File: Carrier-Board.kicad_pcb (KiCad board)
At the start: 4 copper layers, 92 x 96 mm, 50 parts, among them J1 CONN_3-6318491-6, J10 Conn_02x03_Odd_Even, J2 Conn_01x0, J3 Conn_02x26_Odd_Even, J4 SI-51009-F, J5 Conn_02x26_Odd_Even, J6 Conn_01x03_Male, J7 Conn_01x03_Male, J8 Conn_01x06_Male, J9 Conn_02x04_Odd_Even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

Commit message: asdf
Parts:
- removed C1, C3: 10uF, Capacitors_SMD:C_0805
- removed C2, C4: 22uF, Capacitors_SMD:C_0805
- removed C27, C28, C29: .1uF, Capacitors_SMD:C_0603
- removed D5: D_Zener 9V, Diodes_SMD:D_SOD-323
- removed D6, D7, D8: LED, Diodes_SMD:D_1206
- removed G1 (x2): LOGO, BusSimulator:LetSatLogo440
- removed J10: Conn_02x03_Odd_Even, Pin_Headers:Pin_Header_Angled_2x03_Pitch2.54mm
- removed J2: Conn_01x0, Connectors:Barrel_Jack_CUI_PJ-036AH-SMT
- removed J4: SI-51009-F, Carrier-Board:SI-51009-F
- removed J6, J7: Conn_01x03_Male, Pin_Headers:Pin_Header_Angled_1x03_Pitch2.54mm
- removed J8: Conn_01x06_Male, Pin_Headers:Pin_Header_Angled_1x06_Pitch2.54mm
- removed J9: Conn_02x04_Odd_Even, Pin_Headers:Pin_Header_Angled_2x04_Pitch2.54mm
- removed R1, R5: 160k, Resistors_SMD:R_0805
- removed R10, R9: 330, Resistors_SMD:R_0805
- removed R11, R12, R13: 10K, Resistors_SMD:R_0603
- removed R2: 30.1k, Resistors_SMD:R_0805
- removed R23: 330, Resistors_SMD:R_0603
- removed R24: 180, Resistors_SMD:R_0603
- removed R25: 1k, Resistors_SMD:R_0603
- removed R3, R7: 100k, Resistors_SMD:R_0805
- removed R32: 0, Resistors_SMD:R_0805
- removed R4: 63.4k, Resistors_SMD:R_0805
- removed R6: 51k, Resistors_SMD:R_0805
- removed R8: 56k, Resistors_SMD:R_0805
- removed SW1, SW2, SW3: SW_Push, Buttons_Switches_SMD:SW_SPST_B3U-1000P
- removed U1, U2: MPM3620, BusSimulator:QFN-20
- moved U9 218.5 mm to (358.6, 151.7)
- moved J1 217.3 mm to (380.6, 54.9)
- moved J3 217.3 mm to (345.2, 36.8)
- moved J5 217.3 mm to (345.2, 41.8)
- moved m2 217.3 mm to (311.5, 97.2)
- moved m1 217.3 mm to (387.3, 50.2)
- moved m1 217.3 mm to (387.3, 97.2)
- moved REF** 217.3 mm to (301.1, 126.3)
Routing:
- net +3.3V: track 203.6 -> 0.00 mm, vias 6 -> 0
- net GBE0_CTREF(GND): track 166.6 -> 0.00 mm, vias 83 -> 0
- net mCOM_5V_SBY: track 157.2 -> 0.00 mm, vias 4 -> 0
- net mCOM_12V: track 143.3 -> 0.00 mm, vias 3 -> 0
- net PWRBTNn: track 106.5 -> 0.00 mm, vias 3 -> 0
- net SYS_RESETn: track 88.2 -> 0.00 mm, vias 4 -> 0
- net GPI0: track 84.5 -> 0.00 mm, vias 1 -> 0
- net GBE0_MDI2+: track 81.4 -> 0.00 mm, vias 2 -> 0
- net GBE0_MDI2-: track 81.1 -> 0.00 mm, vias 2 -> 0
- net GBE0_MDI3-: track 81.0 -> 0.00 mm, vias 2 -> 0
- net GBE0_MDI1-: track 81.0 -> 0.00 mm, vias 2 -> 0
- net GBE0_MDI3+: track 80.7 -> 0.00 mm, vias 2 -> 0
- net GPO1: track 80.5 -> 0.00 mm, vias 1 -> 0
- net GBE0_MDI1+: track 80.1 -> 0.00 mm, vias 2 -> 0
- net GBE0_MDI0-: track 79.5 -> 0.00 mm, vias 2 -> 0
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- removed copper zone on F.Cu, net +3.3V
- removed copper zone on B.Cu, net GBE0_CTREF(GND)
- removed copper zone on F.Cu, net GBE0_CTREF(GND)
- removed copper zone on In1.Cu, net GBE0_CTREF(GND)
- removed copper zone on In2.Cu, net GBE0_CTREF(GND)
- removed copper zone on F.Cu, net mCOM_12V
- removed copper zone on F.Cu, net mCOM_5V_SBY
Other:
- board text removed: "S/N: 00000000"
- board text removed: "mCOM-TK1 Carrier Board"

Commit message: removed stuff we dont need
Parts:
- removed m1 (x2), m2: MountingHole_2.7mm_M2.5_Pad, Mounting_Holes:MountingHole_2.7mm_M2.5_Pad
- added C27: .1uF, Capacitors_SMD:C_0603, F.Cu at (160.7, 82.1)
- added C28: .1uF, Capacitors_SMD:C_0603, F.Cu at (160.7, 75.4)
- added C29: .1uF, Capacitors_SMD:C_0603, F.Cu at (161.3, 63.1)
- added G1: LOGO, BusSimulator:LetSatLogo440, B.Cu at (125.6, 93.7)
- added G1: LOGO, BusSimulator:LetSatLogo440, F.Cu at (126.7, 70.2)
- added R32: 0, Resistors_SMD:R_0805, B.Cu at (168.2, 83.6)
- moved U9 218.5 mm to (161.3, 57.8)
- moved J1 217.3 mm to (163.5, 48.5)
- moved J3 217.3 mm to (128.0, 30.4)
- moved J5 217.3 mm to (128.0, 35.5)
- moved REF** 217.3 mm to (83.9, 120.0)
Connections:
- J1 pad 1: GBE0_CTREF(GND) -> mCOM_GND
- J1 pad 100: GBE0_CTREF(GND) -> mCOM_GND
- J1 pad 11: GBE0_CTREF(GND) -> mCOM_GND
- J1 pad 110: GBE0_CTREF(GND) -> mCOM_GND
- J1 pad 111: GBE0_CTREF(GND) -> mCOM_GND
- J1 pad 121: GBE0_CTREF(GND) -> mCOM_GND
- J1 pad 131: GBE0_CTREF(GND) -> mCOM_GND
- J1 pad 141: GBE0_CTREF(GND) -> mCOM_GND
- J1 pad 151: GBE0_CTREF(GND) -> mCOM_GND
- J1 pad 161: GBE0_CTREF(GND) -> mCOM_GND
- J1 pad 170: GBE0_CTREF(GND) -> mCOM_GND
- J1 pad 180: GBE0_CTREF(GND) -> mCOM_GND
- J1 pad 190: GBE0_CTREF(GND) -> mCOM_GND
- J1 pad 200: GBE0_CTREF(GND) -> mCOM_GND
- J1 pad 21: GBE0_CTREF(GND) -> mCOM_GND
- J1 pad 210: GBE0_CTREF(GND) -> mCOM_GND
- J1 pad 220: GBE0_CTREF(GND) -> mCOM_GND
- J1 pad 223: GBE0_CTREF(GND) -> (no net)
- J1 pad 224: GBE0_CTREF(GND) -> (no net)
- J1 pad 31: GBE0_CTREF(GND) -> mCOM_GND
- J1 pad 41: GBE0_CTREF(GND) -> mCOM_GND
- J1 pad 51: GBE0_CTREF(GND) -> mCOM_GND
- J1 pad 57: GBE0_CTREF(GND) -> mCOM_GND
- J1 pad 60: GBE0_CTREF(GND) -> mCOM_GND
- J1 pad 66: GBE0_CTREF(GND) -> mCOM_GND
- J1 pad 70: GBE0_CTREF(GND) -> mCOM_GND
- J1 pad 80: GBE0_CTREF(GND) -> mCOM_GND
- J1 pad 90: GBE0_CTREF(GND) -> mCOM_GND
- U9 pad 15: GBE0_CTREF(GND) -> GNDREF
- U9 pad 18: GBE0_CTREF(GND) -> GNDREF
- U9 pad 21: GBE0_CTREF(GND) -> GNDREF
- U9 pad 26: GBE0_CTREF(GND) -> GNDREF
- U9 pad 27: GBE0_CTREF(GND) -> GNDREF
- U9 pad 29: GBE0_CTREF(GND) -> GNDREF
- U9 pad 34: GBE0_CTREF(GND) -> GNDREF
- U9 pad 35: GBE0_CTREF(GND) -> GNDREF
- U9 pad 37: GBE0_CTREF(GND) -> GNDREF
- U9 pad 4: GBE0_CTREF(GND) -> GNDREF
- U9 pad 40: GBE0_CTREF(GND) -> GNDREF
- U9 pad 50: GBE0_CTREF(GND) -> GNDREF
- U9 pad 9: GBE0_CTREF(GND) -> GNDREF
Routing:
- net GNDREF: track 0.00 -> 0.58 mm
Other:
- board text added: "S/N: 00000000"
- board text added: "mCOM-TK1 Carrier Board"

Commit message: stuff
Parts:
- removed the REF** at (83.9, 120.0)
- added REF**: LetSat1PCB, Carrier-Board:LetSat1PCB, F.Cu at (83.9, 120.0)
- moved J3 0.07 mm to (127.9, 30.4)
- moved J5 0.07 mm to (127.9, 35.5)
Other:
- outline, holes or cut-outs redrawn
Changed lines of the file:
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@@
 (kicad_pcb (version 4) (host pcbnew 4.0.7)
   (general
-    (links 68)
+    (links 0)
     (no_connects 68)
-    (area 0 0 0 0)
+    (area 71.837143 23.749999 174.170001 124.545)
     (thickness 1.6)
     (drawings 2)
@@
     (34 B.Paste user)
     (35 F.Paste user)
-    (36 B.SilkS user)
+    (36 B.SilkS user hide)
     (37 F.SilkS user)
-    (38 B.Mask user)
-    (39 F.Mask user)
+    (38 B.Mask user hide)
+    (39 F.Mask user hide)
     (40 Dwgs.User user)
     (41 Cmts.User user)
@@
     (aux_axis_origin 0 0)
     (grid_origin 128.775 45.85)
-    (visible_elements 7FFFE7FF)
+    (visible_elements 7FFFF7FF)
     (pcbplotparams
       (layerselection 0x00030_80000001)
@@
     )
   )
-  (module Carrier-Board:pc104 locked (layer F.Cu)
-    (at 83.92 120)
-    (fp_text reference REF** (at 0.75 -97.5) (layer F.SilkS)
-      (effects (font (size 1 1) (thickness 0.15)))
-    )
-    (fp_text value pc104 (at 0 -0.525) (layer F.Fab)
-      (effects (font (size 1 1) (thickness 0.15)))
-    )
-    (fp_arc (start 90 -51) (end 90 -53) (angle -90) (layer Edge.Cuts) (width 0.1))
-    (fp_line (start 26.8 -93) (end 15 -93) (layer Edge.Cuts) (width 0.1))
-    (fp_arc (start 62 0) (end 65 0) (angle -90) (layer Edge.Cuts) (width 0.1))
-    (fp_arc (start -2 -51) (end 0 -51) (angle -90) (layer Edge.Cuts) (width 0.1))
-    (fp_circle (center 80.9 -90.9) (end 82.5 -90.9) (layer Edge.Cuts) (width 0.1))
-    (fp_circle (center 83.4 -5.2) (end 85 -5.2) (layer Edge.Cuts) (width 0.1))
-    (fp_line (start 38.2 -3) (end 62 -3) (layer Edge.Cuts) (width 0.1))
-    (fp_circle (center 7.2 -90.9) (end 8.8 -90.9) (layer Edge.Cuts) (width 0.1))
-    (fp_line (start 88 0) (end 88 -11) (layer Edge.Cuts) (width 0.1))
-    (fp_line (start 0 -16) (end 0 0) (layer Edge.Cuts) (width 0.1))
-    (fp_circle (center 3.4 -5.2) (end 5 -5.2) (layer Edge.Cuts) (width 0.1))
-    (fp_line (start 12 -96) (end 0 -96) (layer Edge.Cuts) (width 0.1))
-    (fp_line (start 0 -51) (end 0 -45) (layer Edge.Cuts) (width 0.1))
-    (fp_arc (start 15 -96) (end 12 -96) (angle -90) (layer Edge.Cuts) (width 0.1))
-    (fp_arc (start -2 -85) (end -2 -83) (angle -90) (layer Edge.Cuts) (width 0.1))
-    (fp_line (start 90 -13) (end 90 -43) (layer Edge.Cuts) (width 0.1))
-    (fp_arc (start 90 -88) (end 89 -88) (angle -90) (layer Edge.Cuts) (width 0.1))
-    (fp_line (start -2 -43) (end -2 -18) (layer Edge.Cuts) (width 0.1))
-    (fp_line (start -2 -83) (end -2 -53) (layer Edge.Cuts) (width 0.1))
-    (fp_line (start 89 -88) (end 89 -96) (layer Edge.Cuts) (width 0.1))
-    (fp_arc (start 90 -11) (end 90 -13) (angle -90) (layer Edge.Cuts) (width 0.1))
-    (fp_arc (start 26.8 -96) (end 26.8 -93) (angle -90) (layer Edge.Cuts) (width 0.1))
-    (fp_line (start 90 -53) (end 90 -87) (layer Edge.Cuts) (width 0.1))
-    (fp_arc (start 38.2 0) (end 38.2 -3) (angle -90) (layer Edge.Cuts) (width 0.1))
-    (fp_arc (start -2 -45) (end -2 -43) (angle -90) (layer Edge.Cuts) (width 0.1))
-    (fp_line (start 89 -96) (end 29.8 -96) (layer Edge.Cuts) (width 0.1))
-    (fp_line (start 65 0) (end 88 0) (layer Edge.Cuts) (width 0.1))
-    (fp_line (start 0 0) (end 35.2 0) (layer Edge.Cuts) (width 0.1))
-    (fp_line (start 0 -96) (end 0 -85) (layer Edge.Cuts) (width 0.1))
-    (fp_arc (start -2 -16) (end 0 -16) (angle -90) (layer Edge.Cuts) (width 0.1))
-    (fp_arc (start 90 -45) (end 88 -45) (angle -90) (layer Edge.Cuts) (width 0.1))
-    (fp_line (start 88 -45) (end 88 -51) (layer Edge.Cuts) (width 0.1))
-  )
   (module BusSimulator:LetSatLogo440 (layer F.Cu)
     (at 126.655 70.19)
@@
   )
   (module Carrier-Board:ESQ-126-XX-X-D locked (layer F.Cu)
-    (at 128.01 35.485)
+    (at 127.949 35.454)
     (descr "ELEVATED SOCKET, .100 INCH(2.54MM) PITCH")
     (tags "ELEVATED SOCKET, .100 INCH(2.54MM) PITCH")
     (attr virtual)
-    (fp_text reference J5 (at 0 0) (layer F.SilkS)
+    (fp_text reference J5 (at 0 0) (layer F.SilkS) hide
       (effects (font (thickness 0.15)))
     )
-    (fp_text value Conn_02x26_Odd_Even (at -0.084001 -0.343961) (layer F.SilkS)
+    (fp_text value Conn_02x26_Odd_Even (at -0.084001 -0.343961) (layer F.SilkS) hide
       (effects (font (thickness 0.15)))
     )
@@
   )
   (module Carrier-Board:ESQ-126-XX-X-D locked (layer F.Cu)
-    (at 128.009001 30.408961)
+    (at 127.948001 30.377961)
     (descr "ELEVATED SOCKET, .100 INCH(2.54MM) PITCH")
     (tags "ELEVATED SOCKET, .100 INCH(2.54MM) PITCH")
     (attr virtual)
-    (fp_text reference J3 (at 0 0) (layer F.SilkS)
+    (fp_text reference J3 (at 0 0) (layer F.SilkS) hide
       (effects (font (thickness 0.15)))
     )
-    (fp_text value Conn_02x26_Odd_Even (at 0 0) (layer F.SilkS)
+    (fp_text value Conn_02x26_Odd_Even (at 0 0) (layer F.SilkS) hide
       (effects (font (thickness 0.15)))
     )
@@
       (net 1 +3.3V))
   )
+  (module Carrier-Board:LetSat1PCB (layer F.Cu)
+    (at 83.92 120)
+    (fp_text reference REF** (at -9.74 3.47) (layer F.SilkS)
+      (effects (font (size 1 1) (thickness 0.15)))
+    )
+    (fp_text value LetSat1PCB (at 2.245 1.18) (layer F.Fab)
+      (effects (font (size 1 1) (thickness 0.15)))
+    )
+    (fp_circle (center 83.4 -5.2) (end 85 -5.2) (layer Edge.Cuts) (width 0.1))
+    (fp_circle (center 3.4 -5.2) (end 5 -5.2) (layer Edge.Cuts) (width 0.1))
+    (fp_circle (center 7.2 -90.9) (end 8.8 -90.9) (layer Edge.Cuts) (width 0.1))
+    (fp_circle (center 80.9 -90.9) (end 82.5 -90.9) (layer Edge.Cuts) (width 0.1))
+    (fp_circle (center 75.78 -83.28) (end 76.28 -83.28) (layer Dwgs.User) (width 0.1))
+    (fp_circle (center 12.28 -90.9) (end 12.78 -90.9) (layer Dwgs.User) (width 0.1))
+    (fp_arc (start -2 -16) (end 0 -16) (angle -90) (layer Edge.Cuts) (width 0.1))
+    (fp_line (start 14.37 -3) (end 72.43 -3) (layer Edge.Cuts) (width 0.1))
+    (fp_line (start 0 0) (end 11.37 0) (layer Edge.Cuts) (width 0.1))
+    (fp_line (start 0 -96) (end 0 -85) (layer Edge.Cuts) (width 0.1))
+    (fp_line (start 0 -63.000416) (end 0 -33.000416) (layer Edge.Cuts) (width 0.1))
+    (fp_line (start 75.43 0) (end 88 0) (layer Edge.Cuts) (width 0.1))
+    (fp_line (start -2 -83) (end -2 -65.000416) (layer Edge.Cuts) (width 0.1))
+    (fp_arc (start -2 -33.000416) (end -2 -31.000416) (angle -90) (layer Edge.Cuts) (width 0.1))
+    (fp_line (start 88 0) (end 88 -11) (layer Edge.Cuts) (width 0.1))
+    (fp_arc (start 90 -63.000416) (end 90 -65.000416) (angle -90) (layer Edge.Cuts) (width 0.1))
+    (fp_line (start 89 -96) (end 76.06 -96) (layer Edge.Cuts) (width 0.1))
+    (fp_line (start -2 -31.000416) (end -2 -18) (layer Edge.Cuts) (width 0.1))
+    (fp_arc (start 14.37 0) (end 14.37 -3) (angle -90) (layer Edge.Cuts) (width 0.1))
+    (fp_arc (start -2 -85) (end -2 -83) (angle -90) (layer Edge.Cuts) (width 0.1))
+    (fp_line (start 0 -4.369338) (end 0 0) (layer Edge.Cuts) (width 0.1))
+    (fp_line (start 88 -33.000416) (end 88 -63.000416) (layer Edge.Cuts) (width 0.1))
+    (fp_line (start 89 -88) (end 89 -96) (layer Edge.Cuts) (width 0.1))
+    (fp_arc (start 15 -96) (end 12 -96) (angle -90) (layer Edge.Cuts) (width 0.1))
+    (fp_arc (start 90 -33.000416) (end 88 -33.000416) (angle -90) (layer Edge.Cuts) (width 0.1))
+    (fp_arc (start 90 -88) (end 89 -88) (angle -90) (layer Edge.Cuts) (width 0.1))
+    (fp_line (start 73.06 -93) (end 15 -93) (layer Edge.Cuts) (width 0.1))
+    (fp_arc (start -2 -63.000416) (end 0 -63.000416) (angle -90) (layer Edge.Cuts) (width 0.1))
+    (fp_arc (start 3.4 -5.2) (end 0 -6.030662) (angle -27.45826535) (layer Edge.Cuts) (width 0.1))
+    (fp_arc (start 72.43 0) (end 75.43 0) (angle -90) (layer Edge.Cuts) (width 0.1))
+    (fp_arc (start 90 -11) (end 90 -13) (angle -90) (layer Edge.Cuts) (width 0.1))
+    (fp_line (start 90 -13) (end 90 -31.000416) (layer Edge.Cuts) (width 0.1))
+    (fp_line (start 90 -65.000416) (end 90 -87) (layer Edge.Cuts) (width 0.1))
+    (fp_arc (start 73.06 -96) (end 73.06 -93) (angle -90) (layer Edge.Cuts) (width 0.1))
+    (fp_line (start 0 -16) (end 0 -6.030662) (layer Edge.Cuts) (width 0.1))
+    (fp_line (start 12 -96) (end 0 -96) (layer Edge.Cuts) (width 0.1))
+  )
   (gr_text "S/N: 00000000" (at 113.25 107) (layer B.SilkS)

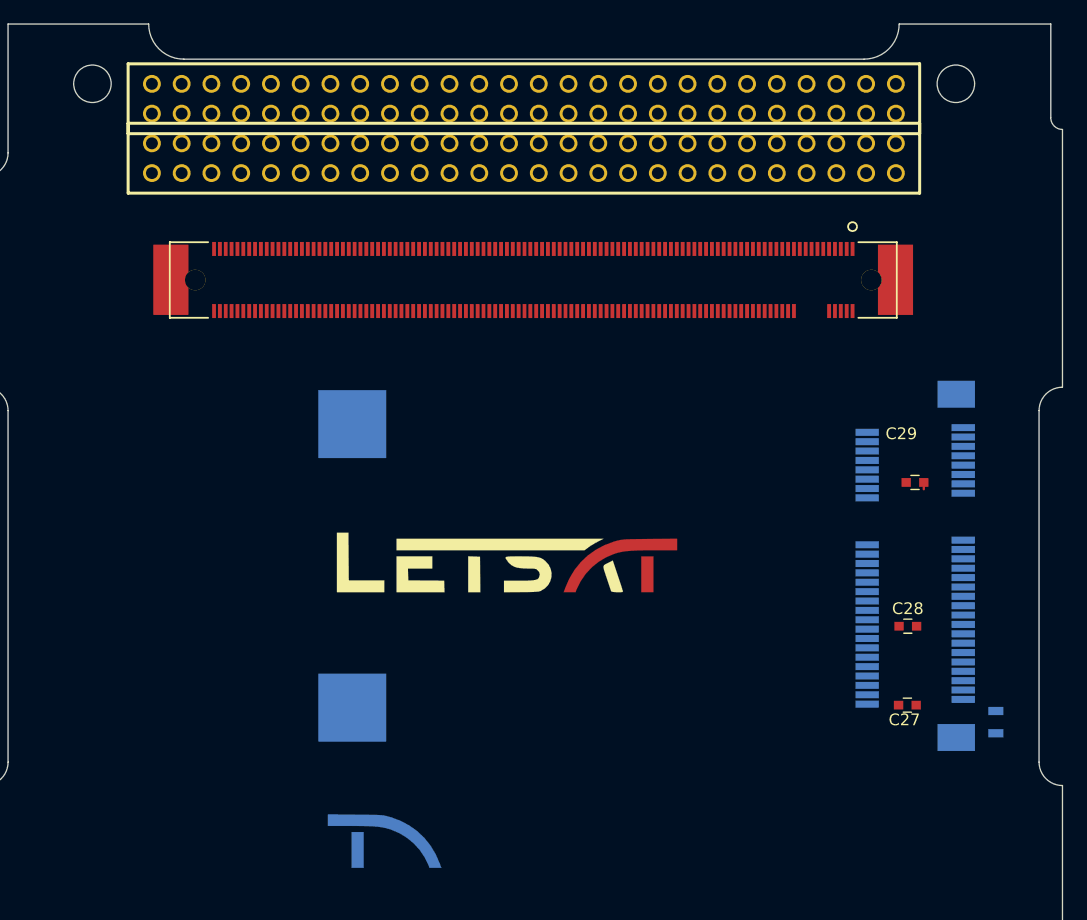
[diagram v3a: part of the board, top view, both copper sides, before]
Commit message: Update mCOM connector, correct header refs/silk
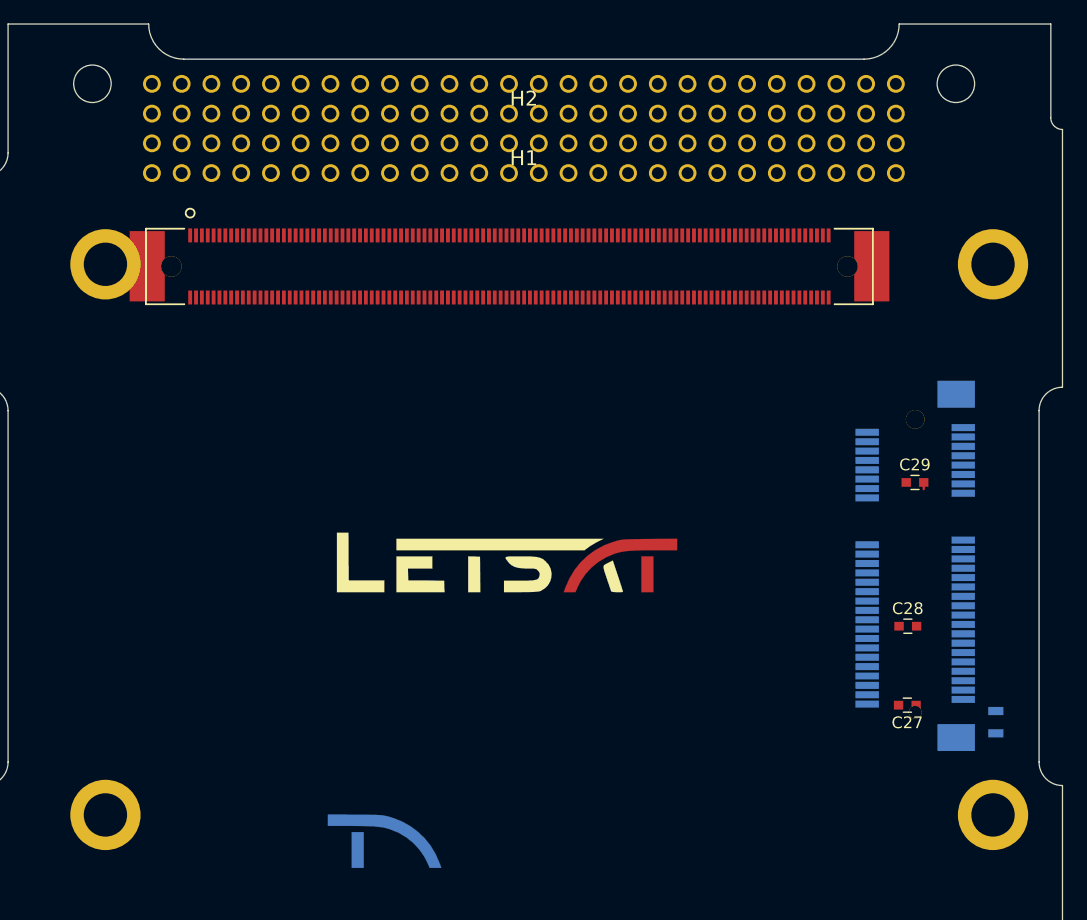
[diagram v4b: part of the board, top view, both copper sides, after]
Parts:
- J1: footprint BusSimulator:ComExpressMini10 -> Carrier-Board:MCOM10-K1; moved to B.Cu
- moved J1 71.4 mm to (92.2, 44.5), turned to 0 degrees
- renumbered J5 to H1, J3 to H2
